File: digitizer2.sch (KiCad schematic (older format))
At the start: 209 parts, among them P1 USB_OTG, P2 CONN_01X01, P3 CONN_01X01, P4 SMA, P5 SMA, P6 SMA, P7 CONN_02X03, P8 CONN_02X03, T1 ETC1-1-13, T2 ETC1-1-13, U1 XC7A35T, U10 SN65LVDS100DGK, U11 SN65LVDS100DGK, U12 ASG2-D-X-A-500.000MHZ, U16 FXO-LC526R-100, U2 FT2232H-56Q, U3 MT41J128M16, U4 ADS5403, U5 TPS79625DCQ, U6 TPS79618DCQ, U7 TPS79633DCQ, U8 93LC46BT-I/OT, Y1 ABM8G-12.000MHZ-18-D2Y-T

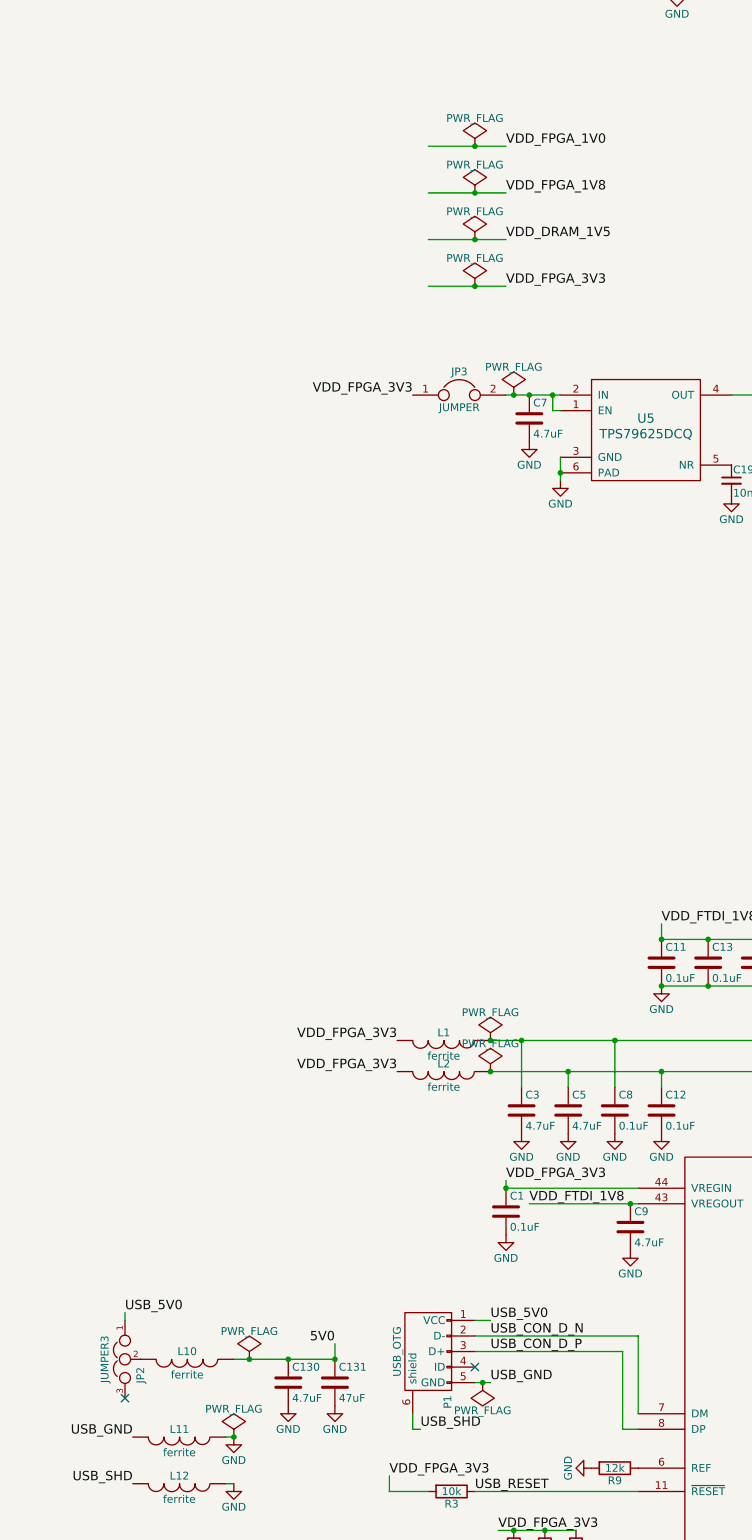
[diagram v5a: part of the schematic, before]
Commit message: Move power supply off-board
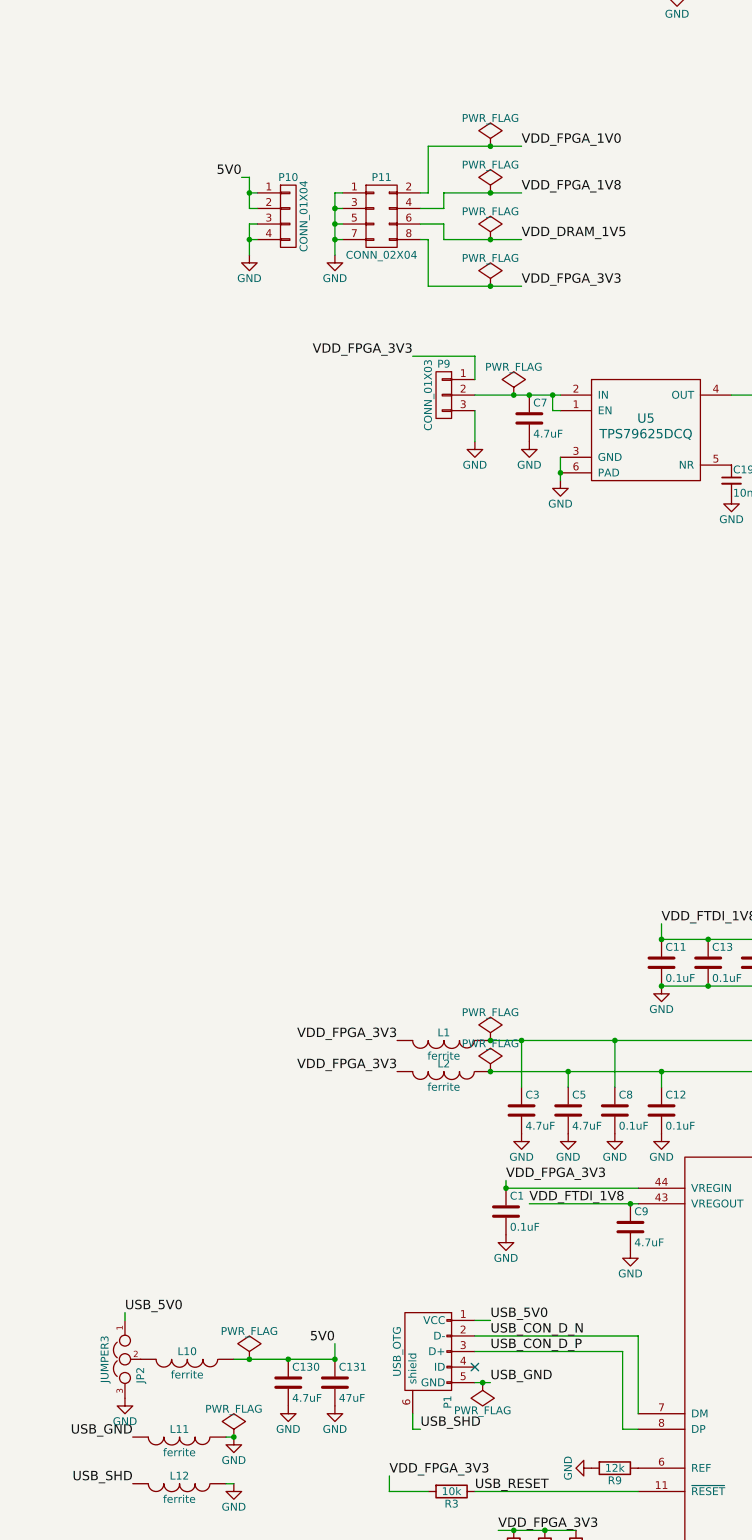
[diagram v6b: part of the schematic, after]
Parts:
- removed JP3: JUMPER, Pin_Headers:Pin_Header_Straight_1x02, symbol JUMPER
- added P10: CONN_01X04, Pin_Headers:Pin_Header_Straight_1x04, symbol CONN_01X04
- added P11: CONN_02X04, Pin_Headers:Pin_Header_Straight_2x04, symbol CONN_02X04
- added P9: CONN_01X03, Pin_Headers:Pin_Header_Straight_1x03, symbol CONN_01X03
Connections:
- net 5V0: now also P10.1 (P1), P10.2 (P2)
- net GND: now also JP2.3, P10.3 (P3), P10.4 (P4), P11.1 (P1), P11.3 (P3), P11.5 (P5), P11.7 (P7), P9.3 (P3)
- net VDD_DRAM_1V5: now also P11.6 (P6)
- net VDD_FPGA_1V0: now also P11.2 (P2)
- net VDD_FPGA_1V8: now also P11.4 (P4)
- net VDD_FPGA_3V3: now also P11.8 (P8), P9.1 (P1)
- net at C7.1, U5.1 (EN), U5.2 (IN): now also P9.2 (P2)
- no-connect marks 75 -> 74
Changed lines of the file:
@@
 	0    1    1    0
 $EndComp
-NoConn ~ -850 16850
 $Comp
 L GND #PWR049
@@
 Wire Wire Line
 	2700 7450 4450 7450
-Connection ~ 1400 9700
-Connection ~ 1400 9400
-Connection ~ 1400 9100
-Connection ~ 1400 8800
+Connection ~ 1500 9700
+Connection ~ 1500 9400
+Connection ~ 1500 9100
+Connection ~ 1500 8800
 Wire Wire Line
-	1100 9700 1600 9700
+	1100 9700 1700 9700
 Wire Wire Line
-	1100 9400 1600 9400
+	1200 9400 1700 9400
 Wire Wire Line
-	1100 9100 1600 9100
+	1200 9100 1700 9100
 $Comp
 L PWR_FLAG #FLG0109
 U 1 1 57770FC5
-P 1400 8800
-F 0 "#FLG0109" H 1400 8895 50  0001 C CNN
-F 1 "PWR_FLAG" H 1400 8980 50  0000 C CNN
-F 2 "" H 1400 8800 50  0000 C CNN
-F 3 "" H 1400 8800 50  0000 C CNN
-	1    1400 8800
+P 1500 8800
+F 0 "#FLG0109" H 1500 8895 50  0001 C CNN
+F 1 "PWR_FLAG" H 1500 8980 50  0000 C CNN
+F 2 "" H 1500 8800 50  0000 C CNN
+F 3 "" H 1500 8800 50  0000 C CNN
+	1    1500 8800
 	1    0    0    -1
 $EndComp
@@
 L PWR_FLAG #FLG0110
 U 1 1 5775CAB7
-P 1400 9100
-F 0 "#FLG0110" H 1400 9195 50  0001 C CNN
-F 1 "PWR_FLAG" H 1400 9280 50  0000 C CNN
-F 2 "" H 1400 9100 50  0000 C CNN
-F 3 "" H 1400 9100 50  0000 C CNN
-	1    1400 9100
+P 1500 9100
+F 0 "#FLG0110" H 1500 9195 50  0001 C CNN
+F 1 "PWR_FLAG" H 1500 9280 50  0000 C CNN
+F 2 "" H 1500 9100 50  0000 C CNN
+F 3 "" H 1500 9100 50  0000 C CNN
+	1    1500 9100
 	1    0    0    -1
 $EndComp
@@
 L PWR_FLAG #FLG0111
 U 1 1 57753C23
-P 1400 9700
-F 0 "#FLG0111" H 1400 9795 50  0001 C CNN
-F 1 "PWR_FLAG" H 1400 9880 50  0000 C CNN
-F 2 "" H 1400 9700 50  0000 C CNN
-F 3 "" H 1400 9700 50  0000 C CNN
-	1    1400 9700
+P 1500 9700
+F 0 "#FLG0111" H 1500 9795 50  0001 C CNN
+F 1 "PWR_FLAG" H 1500 9880 50  0000 C CNN
+F 2 "" H 1500 9700 50  0000 C CNN
+F 3 "" H 1500 9700 50  0000 C CNN
+	1    1500 9700
 	1    0    0    -1
 $EndComp
@@
 L PWR_FLAG #FLG0112
 U 1 1 5774EA16
-P 1400 9400
-F 0 "#FLG0112" H 1400 9495 50  0001 C CNN
-F 1 "PWR_FLAG" H 1400 9580 50  0000 C CNN
-F 2 "" H 1400 9400 50  0000 C CNN
-F 3 "" H 1400 9400 50  0000 C CNN
-	1    1400 9400
+P 1500 9400
+F 0 "#FLG0112" H 1500 9495 50  0001 C CNN
+F 1 "PWR_FLAG" H 1500 9580 50  0000 C CNN
+F 2 "" H 1500 9400 50  0000 C CNN
+F 3 "" H 1500 9400 50  0000 C CNN
+	1    1500 9400
 	1    0    0    -1
 $EndComp
-Text Label 1600 9400 0    60   ~ 0
+Text Label 1700 9400 0    60   ~ 0
 VDD_DRAM_1V5
-Text Label 1600 9100 0    60   ~ 0
+Text Label 1700 9100 0    60   ~ 0
 VDD_FPGA_1V8
-Text Label 1600 8800 0    60   ~ 0
+Text Label 1700 8800 0    60   ~ 0
 VDD_FPGA_1V0
-Text Label 1600 9700 0    60   ~ 0
+Text Label 1700 9700 0    60   ~ 0
 VDD_FPGA_3V3
 Wire Wire Line
-	1100 8800 1600 8800
+	1100 8800 1700 8800
 $Comp
 L TPS79618DCQ U5
@@
 	1900 10400 1900 10500
 Connection ~ 1900 10400
-Text Label 1000 10400 2    60   ~ 0
+Text Label 1000 10150 2    60   ~ 0
 VDD_FPGA_3V3
 Wire Wire Line
-	1600 10400 1950 10400
+	1400 10400 1950 10400
 Text Label 3700 10400 0    60   ~ 0
 VDD_FPGA_2V5
@@
 Connection ~ 3600 28500
 $Comp
-L JUMPER JP3
-U 1 1 57A3CFBA
-P 1300 10400
-F 0 "JP3" H 1300 10550 50  0000 C CNN
-F 1 "JUMPER" H 1300 10320 50  0000 C CNN
-F 2 "Pin_Headers:Pin_Header_Straight_1x02" H 1300 10400 50  0001 C CNN
-F 3 "" H 1300 10400 50  0000 C CNN
-	1    1300 10400
-	1    0    0    -1
-$EndComp
-$Comp
 L PWR_FLAG #FLG0118
 U 1 1 57A40865
@@
 $EndComp
 Connection ~ 1650 10400
+$Comp
+L CONN_01X03 P9
+U 1 1 57982CBE
+P 1200 10400
+F 0 "P9" H 1200 10600 50  0000 C CNN
+F 1 "CONN_01X03" V 1300 10400 50  0000 C CNN
+F 2 "Pin_Headers:Pin_Header_Straight_1x03" H 1200 10400 50  0001 C CNN
+F 3 "" H 1200 10400 50  0000 C CNN
+	1    1200 10400
+	-1   0    0    -1
+$EndComp
+$Comp
+L GND #PWR0119
+U 1 1 57988DBA
+P 1400 10700
+F 0 "#PWR0119" H 1400 10450 50  0001 C CNN
+F 1 "GND" H 1400 10550 50  0000 C CNN
+F 2 "" H 1400 10700 50  0000 C CNN
+F 3 "" H 1400 10700 50  0000 C CNN
+	1    1400 10700
+	1    0    0    -1
+$EndComp
+Wire Wire Line
+	1400 10500 1400 10700
+Wire Wire Line
+	1400 10300 1400 10150
+Wire Wire Line
+	1400 10150 1000 10150
+$Comp
+L GND #PWR0120
+U 1 1 579A9141
+P -850 16850
+F 0 "#PWR0120" H -850 16600 50  0001 C CNN
+F 1 "GND" H -850 16700 50  0000 C CNN
+F 2 "" H -850 16850 50  0000 C CNN
+F 3 "" H -850 16850 50  0000 C CNN
+	1    -850 16850
+	1    0    0    -1
+$EndComp
+$Comp
+L CONN_02X04 P11
+U 1 1 579AE1F2
+P 800 9250
+F 0 "P11" H 800 9500 50  0000 C CNN
+F 1 "CONN_02X04" H 800 9000 50  0000 C CNN
+F 2 "Pin_Headers:Pin_Header_Straight_2x04" H 800 8050 50  0001 C CNN
+F 3 "" H 800 8050 50  0000 C CNN
+	1    800  9250
+	1    0    0    -1
+$EndComp
+Wire Wire Line
+	1100 9700 1100 9400
+Wire Wire Line
+	1100 9400 1050 9400
+Wire Wire Line
+	1200 9400 1200 9300
+Wire Wire Line
+	1200 9300 1050 9300
+Wire Wire Line
+	1200 9100 1200 9200
+Wire Wire Line
+	1200 9200 1050 9200
+Wire Wire Line
+	1100 8800 1100 9100
+Wire Wire Line
+	1100 9100 1050 9100
+$Comp
+L GND #PWR0121
+U 1 1 579B9B37
+P 500 9500
+F 0 "#PWR0121" H 500 9250 50  0001 C CNN
+F 1 "GND" H 500 9350 50  0000 C CNN
+F 2 "" H 500 9500 50  0000 C CNN
+F 3 "" H 500 9500 50  0000 C CNN
+	1    500  9500
+	1    0    0    -1
+$EndComp
+Wire Wire Line
+	550  9100 500  9100
+Wire Wire Line
+	500  9100 500  9500
+Wire Wire Line
+	550  9200 500  9200
+Connection ~ 500  9200
+Wire Wire Line
+	550  9300 500  9300
+Connection ~ 500  9300
+Wire Wire Line
+	550  9400 500  9400
+Connection ~ 500  9400
+$Comp
+L CONN_01X04 P10
+U 1 1 579C1A98
+P 200 9250
+F 0 "P10" H 200 9500 50  0000 C CNN
+F 1 "CONN_01X04" V 300 9250 50  0000 C CNN
+F 2 "Pin_Headers:Pin_Header_Straight_1x04" H 200 9250 50  0001 C CNN
+F 3 "" H 200 9250 50  0000 C CNN
+	1    200  9250
+	1    0    0    -1
+$EndComp
+$Comp
+L GND #PWR0122
+U 1 1 579CBF8D
+P -50 9500
+F 0 "#PWR0122" H -50 9250 50  0001 C CNN
+F 1 "GND" H -50 9350 50  0000 C CNN
+F 2 "" H -50 9500 50  0000 C CNN
+F 3 "" H -50 9500 50  0000 C CNN
+	1    -50  9500
+	1    0    0    -1
+$EndComp
+Wire Wire Line
+	0    9300 -50  9300
+Wire Wire Line
+	-50  9300 -50  9500
+Wire Wire Line
+	0    9400 -50  9400
+Connection ~ -50  9400
+Wire Wire Line
+	0    9200 -50  9200
+Wire Wire Line
+	-50  9200 -50  9000
+Wire Wire Line
+	-50  9000 -100 9000
+Wire Wire Line
+	0    9100 -50  9100
+Connection ~ -50  9100
+Text Label -100 9000 2    60   ~ 0
+5V0
 $EndSCHEMATC

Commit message: Last tweaks for board rev 1.2
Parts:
- removed JP1: JUMPER3, Pin_Headers:Pin_Header_Straight_1x03, symbol JUMPER3
- removed P2, P3: CONN_01X01, Connect:Banana_Jack_1Pin, symbol CONN_01X01
- added C20: 220uF, Capacitors_SMD:c_elec_5x5.7, symbol C_Small
- added JP1: JUMPER, Pin_Headers:Pin_Header_Straight_1x02, symbol JUMPER
- added P2: CONN_01X03, Pin_Headers:Pin_Header_Angled_1x03, symbol CONN_01X03
- added R12, R13: 0, Resistors_SMD:R_0603, symbol R
- C1, C104, C105, C106, C107, C108, C109, C11, C116, C117, C118, C119, C12, C120, C121, C13, C132, C134, C14, C146, C148, C15, C16, C17, C18, C2, C22, C33, C34, C8, C80, C81, C82, C83, C84, C85, C92, C93, C94, C95, C96, C97: MPN (none) -> GRM155R71A104KA01
- C10, C122, C123, C125, C126, C128, C130, C140, C141, C3, C41, C42, C47, C48, C5, C57, C58, C64, C65, C7, C71, C72, C9: MPN (none) -> GRM21BR71A475KA73
- C100, C101, C102, C103, C110, C111, C112, C113, C114, C115, C124, C127, C133, C135, C143, C159, C19, C36, C37, C74, C75, C76, C77, C78, C79, C86, C87, C88, C89, C90, C91, C98, C99: MPN (none) -> GRM155R71C103KA01
- C129, C131, C142, C155, C156, C43, C49, C50, C59, C66, C73: MPN (none) -> GRM32ER70J476ME20L
- C136, C137, C138, C139, C38, C39, C40, C44, C45, C46, C51, C53, C54, C55, C56, C60, C61, C62, C63, C67, C68, C69, C70: MPN (none) -> GRM155R60J474KE19
- R22, R25, R31, R33, R35, R36, R37, R38: footprint Resistors_SMD:R_0402 -> Resistors_SMD:R_0603
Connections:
- net 5V0: now also JP1.1
- net A5V0: now also C20.1
- net EXT5V0: now also L9.2, JP1.2, P2.1 (P1)
- net GND: now also C20.2, P2.2 (P2), P2.3 (P3)
- net VDD_ADC_3V3: now also R13.2; no longer C122.1, U6.2 (IN)
- net VDD_DRAM_1V5: now also P11.4 (P4); no longer P11.6 (P6)
- net VDD_FPGA_1V0: now also P11.8 (P8); no longer P11.2 (P2)
- net VDD_FPGA_1V8: now also P11.6 (P6); no longer P11.4 (P4)
- net VDD_FPGA_2V5: now also R12.2; no longer C18.1, C2.1, U4.B10 (IOVDD)
- net VDD_FPGA_3V3: now also P11.2 (P2); no longer P11.8 (P8)
- new net U6_IN: C122.1, R13.1, U6.2 (IN)
- new net VDD_ADC_IO: C18.1, C2.1, R12.1, U4.B10 (IOVDD)
